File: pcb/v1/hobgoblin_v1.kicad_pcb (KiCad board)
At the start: 2 copper layers, 160 x 115 mm, 60 parts, among them J1 5V, J2 RC2014EXT1, J3 RC2014EXT2, J4 USB_B_Mini, J5 UART, SW1 RESET, SW2 ROMBNK, U1 74LS32, U10 FT232RL, U2 Z80CPU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

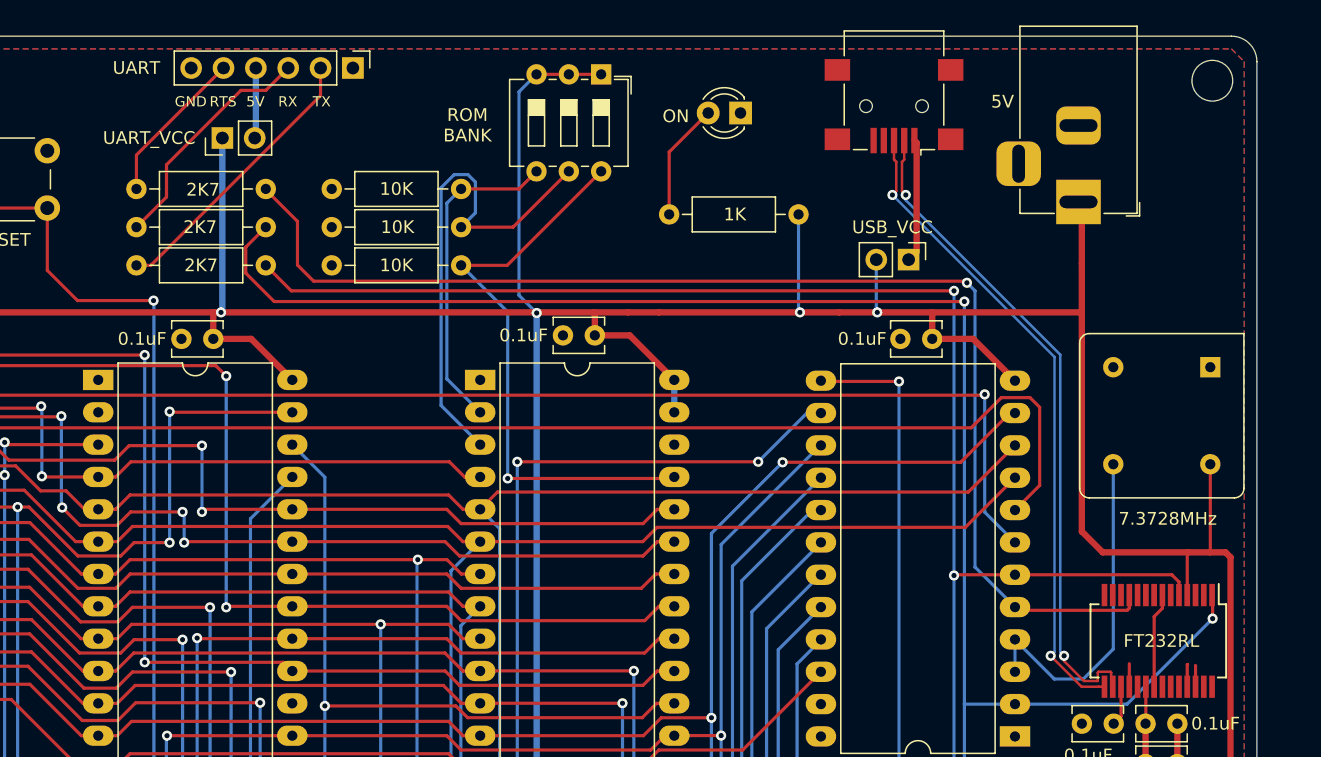
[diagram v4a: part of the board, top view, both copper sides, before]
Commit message: Flip the UART connector
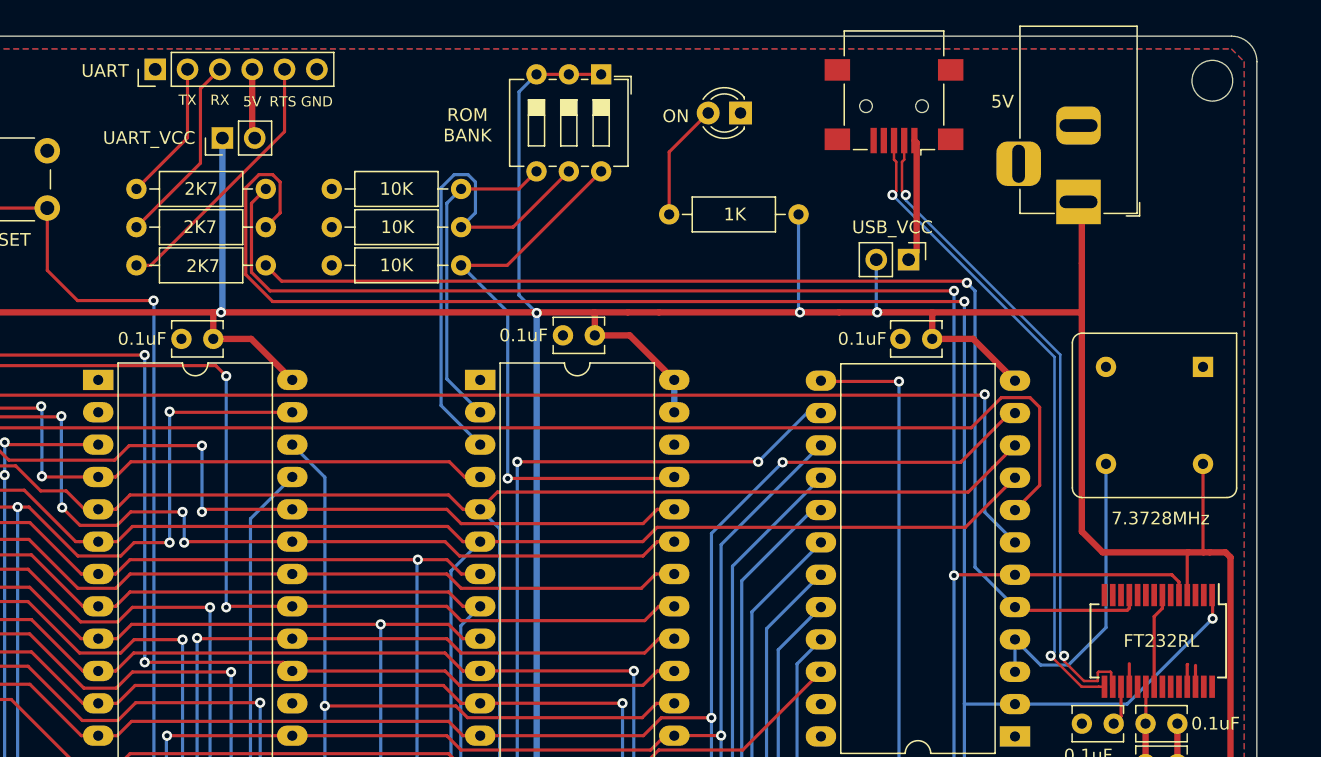
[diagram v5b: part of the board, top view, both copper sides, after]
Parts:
- moved J5 15.5 mm to (93.5, 22.6), turned to 90 degrees
- moved R12 6.00 mm to (92.0, 32.0)
- moved R14 6.00 mm to (92.0, 38.0)
- moved X2 0.57 mm to (175.8, 46.0)
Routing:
- net Net-(J5-Pad2): track 22.2 -> 11.1 mm
- net /RXD: track 317.8 -> 327.7 mm
- net Net-(J5-Pad5): track 12.3 -> 20.9 mm
- net /TXD: track 306.1 -> 314.1 mm
- net /~RTS: track 97.4 -> 92.9 mm
- net Net-(J5-Pad3): track 18.6 -> 15.1 mm
- net /UART_CLK: track 27.0 -> 24.6 mm

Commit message: PCB: final touches
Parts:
- moved X1 0.97 mm to (69.0, 36.1)
- moved C8 0.58 mm to (98.6, 43.8)
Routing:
- net /~MREQ: track 82.1 -> 98.5 mm, vias 3 -> 1
- net VCC: track 660.7 -> 674.4 mm, vias 9 -> 8
- net GND: track 36.5 -> 31.3 mm, vias 3 -> 1
- net Net-(R2-Pad2): track 82.6 -> 79.1 mm, vias 1 -> 0
- net /~MEMWR: track 113.5 -> 110.4 mm, vias 3 -> 2
- net /~PORT38: track 56.9 -> 53.9 mm, vias 1 -> 0
- net /RXD: track 327.7 -> 324.7 mm, vias 4 -> 3
- net /TXD: track 314.1 -> 311.6 mm, vias 4 -> 3
- net /~WR: track 240.4 -> 238.2 mm
- net /~INT: track 223.3 -> 221.1 mm
- net /CPU_CLK: track 87.5 -> 86.8 mm
- net /~IOWR: track 20.6 -> 20.1 mm, vias 2 -> 1
